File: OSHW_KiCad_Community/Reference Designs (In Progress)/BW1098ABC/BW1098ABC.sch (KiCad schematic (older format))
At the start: 10 parts

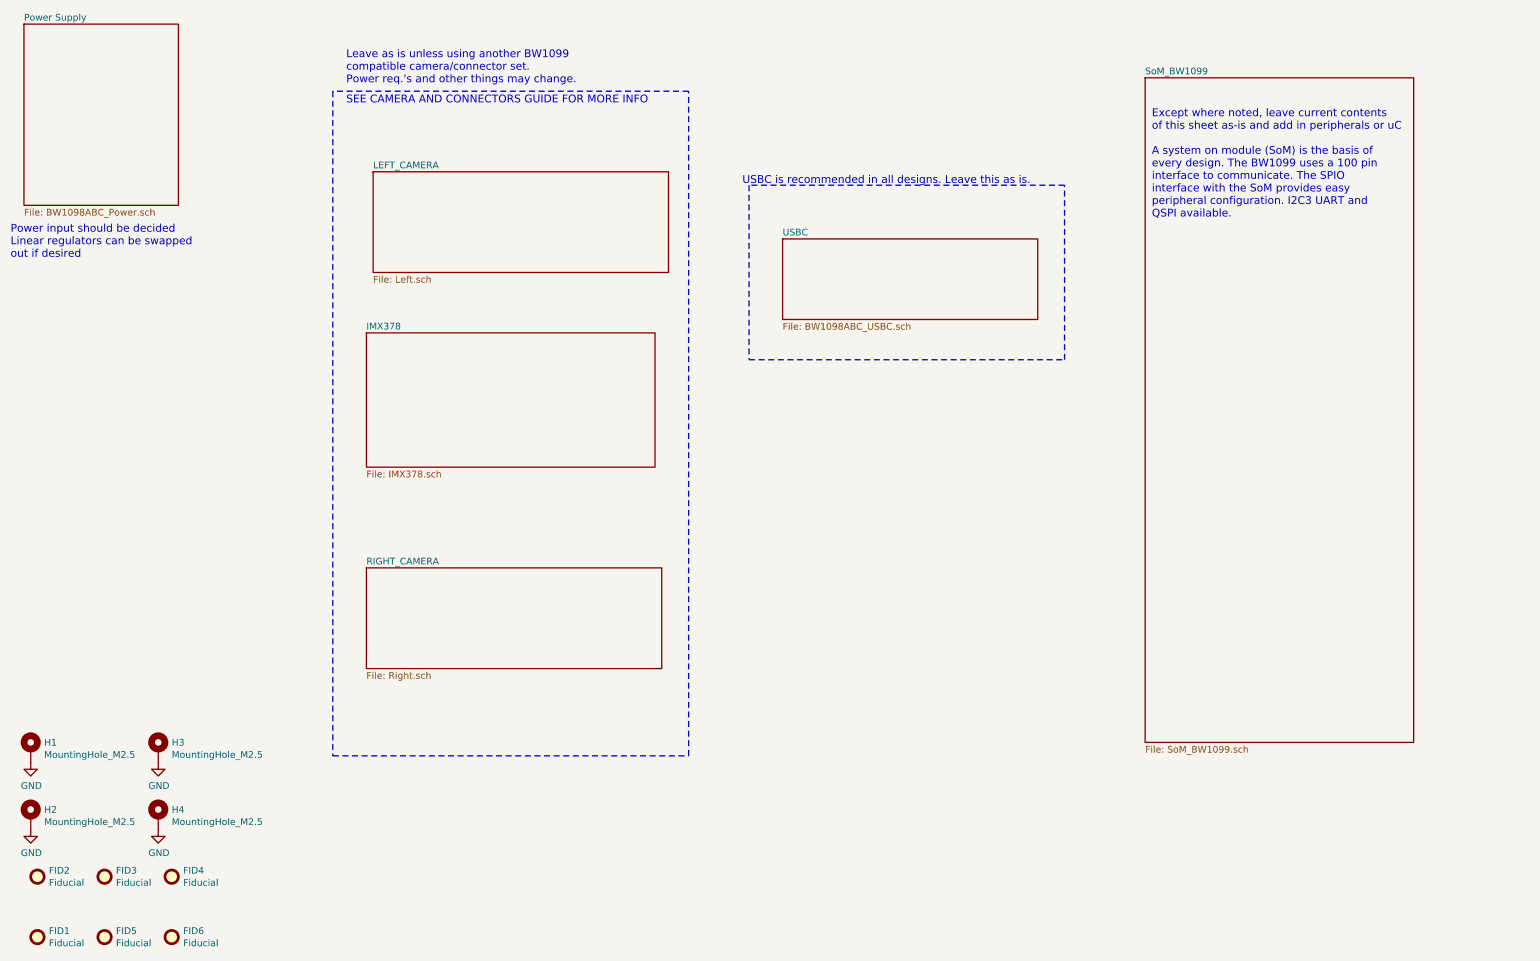
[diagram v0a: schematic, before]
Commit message: switched to ffc design on ABC, dual pop done
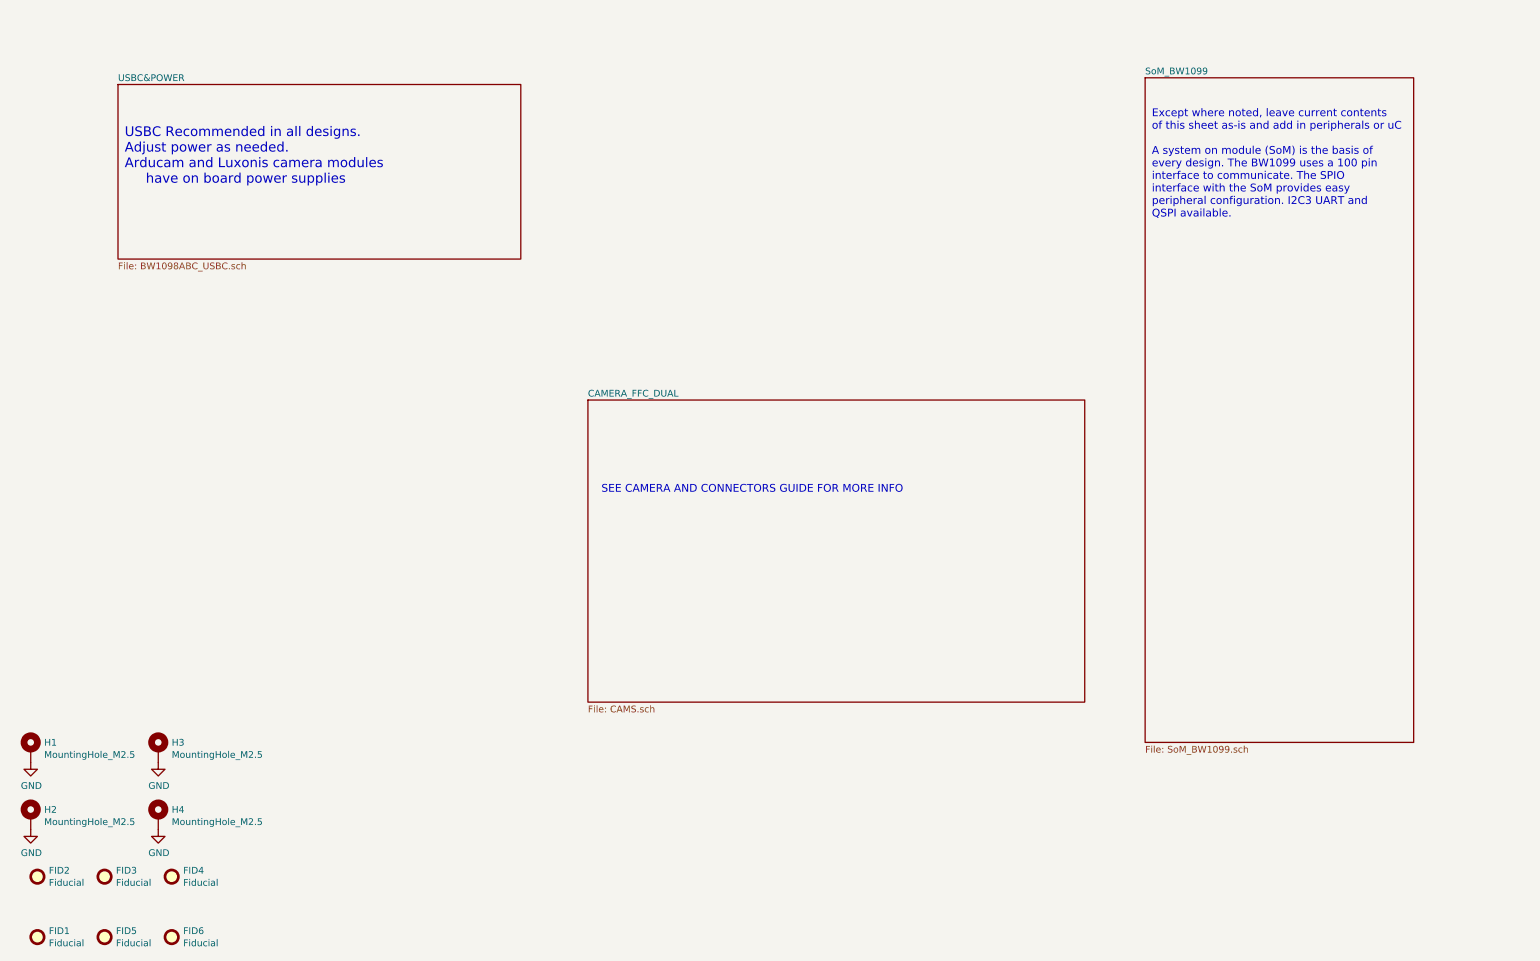
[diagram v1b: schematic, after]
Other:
- note added: "USBC Recommended in all designs. \nAdjust power as needed. \nArducam and Luxonis camera modules \n have on board power supplies"
- note removed: "Leave as is unless using another BW1099 \ncompatible camera/connector set.\nPower req.'s and other things may change."
- note removed: "Power input should be decided\nLinear regulators can be swapped\nout if desired"
- note removed: "USBC is recommended in all designs. Leave this as is.\n"
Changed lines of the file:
@@
 $Descr A4 11693 8268
 encoding utf-8
-Sheet 1 7
+Sheet 1 4
 Title ""
 Date ""
@@
 F0 "SoM_BW1099" 50
 F1 "SoM_BW1099.sch" 50
-$EndSheet
-$Sheet
-S 3150 4650 2200 750
-U 5FF8D40A
-F0 "RIGHT_CAMERA" 50
-F1 "Right.sch" 50
 $EndSheet
 $Comp
@@
 $EndComp
 $Sheet
-S 600  600  1150 1350
-U 604AEAFA
-F0 "Power Supply" 50
-F1 "BW1098ABC_Power.sch" 50
-$EndSheet
-$Sheet
-S 3150 2900 2150 1000
-U 5FF8D4A5
-F0 "IMX378" 50
-F1 "IMX378.sch" 50
-$EndSheet
-$Sheet
-S 3200 1700 2200 750
+S 4800 3400 3700 2250
 U 5FF8D2B3
-F0 "LEFT_CAMERA" 50
-F1 "Left.sch" 50
+F0 "CAMERA_FFC_DUAL" 50
+F1 "CAMS.sch" 50
 $EndSheet
 $Comp
@@
 $EndComp
 $Sheet
-S 6250 2200 1900 600
+S 1300 1050 3000 1300
 U 60483E6B
-F0 "USBC" 50
+F0 "USBC&POWER" 50
 F1 "BW1098ABC_USBC.sch" 50
 $EndSheet
-Wire Notes Line
-	5550 1100 2900 1100
-Wire Notes Line
-	2900 1100 2900 6050
-Wire Notes Line
-	2900 6050 5550 6050
-Wire Notes Line
-	5550 6050 5550 1100
-Text Notes 3000 1200 0    58   ~ 0
+Text Notes 4900 4100 0    58   ~ 0
 SEE CAMERA AND CONNECTORS GUIDE FOR MORE INFO\n
-Wire Notes Line
-	8350 1800 6000 1800
-Wire Notes Line
-	6000 1800 6000 3100
-Wire Notes Line
-	6000 3100 8350 3100
-Wire Notes Line
-	8350 3100 8350 1800
-Text Notes 5950 1800 0    58   ~ 0
-USBC is recommended in all designs. Leave this as is.\n
 Text Notes 9000 2050 0    58   ~ 0
 Except where noted, leave current contents\nof this sheet as-is and add in peripherals or uC\n\nA system on module (SoM) is the basis of \nevery design. The BW1099 uses a 100 pin\ninterface to communicate. The SPIO \ninterface with the SoM provides easy \nperipheral configuration. I2C3 UART and \nQSPI available.
-Text Notes 500  2350 0    58   ~ 0
-Power input should be decided\nLinear regulators can be swapped\nout if desired
-Text Notes 3000 1050 0    58   ~ 0
-Leave as is unless using another BW1099 \ncompatible camera/connector set.\nPower req.'s and other things may change.
+Text Notes 1350 1800 0    72   ~ 0
+USBC Recommended in all designs. \nAdjust power as needed. \nArducam and Luxonis camera modules \n     have on board power supplies
 $EndSCHEMATC

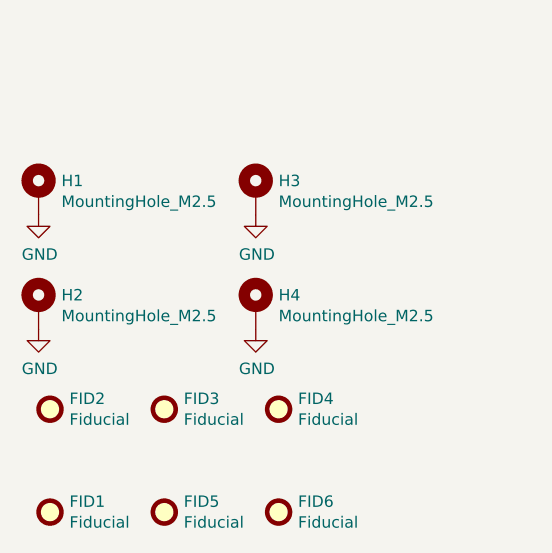
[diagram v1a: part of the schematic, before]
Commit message: added module mounts and started layout for abc
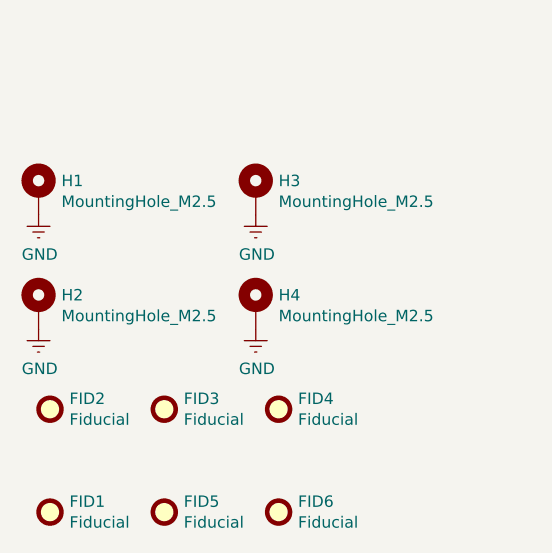
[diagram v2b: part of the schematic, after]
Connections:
- net GND renamed Earth
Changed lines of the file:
@@
 $EndSheet
 $Comp
-L power:GND #PWR0107
+L power:Earth #PWR0107
 U 1 1 6106C817
 P 650 6100
@@
 $EndComp
 $Comp
-L power:GND #PWR0108
+L power:Earth #PWR0108
 U 1 1 6106D903
 P 1600 6100
@@
 $EndComp
 $Comp
-L power:GND #PWR0109
+L power:Earth #PWR0109
 U 1 1 6106E6FC
 P 1600 6600
@@
 $EndComp
 $Comp
-L power:GND #PWR0110
+L power:Earth #PWR0110
 U 1 1 6106EA7D
 P 650 6600

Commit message: layout
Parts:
- added J2: Conn_01x02_Male, Connector_PinHeader_2.54mm:PinHeader_1x02_P2.54mm_Vertical, symbol Connector:Conn_01x02_Male
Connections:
- net Earth: now also J2.1 (Pin_1)
- new net +5V: J2.2 (Pin_2)
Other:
- note added: "FAN CONTROLLER"
- moved on the sheet: FID1, FID2, FID3, FID4, FID5, FID6, H1, H2, H3, H4
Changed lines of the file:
@@
 $EndDescr
 $Sheet
-S 8950 1000 2000 4950
+S 9100 950  2000 4950
 U 5FF8D9B2
 F0 "SoM_BW1099" 50
@@
 L Mechanical:Fiducial FID1
 U 1 1 6049A903
-P 700 7400
-F 0 "FID1" H 785 7446 50  0000 L CNN
-F 1 "Fiducial" H 785 7355 50  0000 L CNN
-F 2 "Fiducial:Fiducial_1mm_Mask2mm" H 700 7400 50  0001 C CNN
-F 3 "~" H 700 7400 50  0001 C CNN
-	1    700  7400
+P 850 7350
+F 0 "FID1" H 935 7396 50  0000 L CNN
+F 1 "Fiducial" H 935 7305 50  0000 L CNN
+F 2 "Fiducial:Fiducial_1mm_Mask2mm" H 850 7350 50  0001 C CNN
+F 3 "~" H 850 7350 50  0001 C CNN
+	1    850  7350
 	1    0    0    -1
 $EndComp
@@
 L Mechanical:Fiducial FID2
 U 1 1 5FF51DEB
-P 700 6950
-F 0 "FID2" H 785 6996 50  0000 L CNN
-F 1 "Fiducial" H 785 6905 50  0000 L CNN
-F 2 "Fiducial:Fiducial_1mm_Mask2mm" H 700 6950 50  0001 C CNN
-F 3 "~" H 700 6950 50  0001 C CNN
-	1    700  6950
+P 850 6900
+F 0 "FID2" H 935 6946 50  0000 L CNN
+F 1 "Fiducial" H 935 6855 50  0000 L CNN
+F 2 "Fiducial:Fiducial_1mm_Mask2mm" H 850 6900 50  0001 C CNN
+F 3 "~" H 850 6900 50  0001 C CNN
+	1    850  6900
 	1    0    0    -1
 $EndComp
@@
 L Mechanical:Fiducial FID3
 U 1 1 6049A905
-P 1200 6950
-F 0 "FID3" H 1285 6996 50  0000 L CNN
-F 1 "Fiducial" H 1285 6905 50  0000 L CNN
-F 2 "Fiducial:Fiducial_1mm_Mask2mm" H 1200 6950 50  0001 C CNN
-F 3 "~" H 1200 6950 50  0001 C CNN
-	1    1200 6950
+P 1350 6900
+F 0 "FID3" H 1435 6946 50  0000 L CNN
+F 1 "Fiducial" H 1435 6855 50  0000 L CNN
+F 2 "Fiducial:Fiducial_1mm_Mask2mm" H 1350 6900 50  0001 C CNN
+F 3 "~" H 1350 6900 50  0001 C CNN
+	1    1350 6900
 	1    0    0    -1
 $EndComp
@@
 L Mechanical:Fiducial FID4
 U 1 1 6049A906
-P 1700 6950
-F 0 "FID4" H 1785 6996 50  0000 L CNN
-F 1 "Fiducial" H 1785 6905 50  0000 L CNN
-F 2 "Fiducial:Fiducial_1mm_Mask2mm" H 1700 6950 50  0001 C CNN
-F 3 "~" H 1700 6950 50  0001 C CNN
-	1    1700 6950
+P 1850 6900
+F 0 "FID4" H 1935 6946 50  0000 L CNN
+F 1 "Fiducial" H 1935 6855 50  0000 L CNN
+F 2 "Fiducial:Fiducial_1mm_Mask2mm" H 1850 6900 50  0001 C CNN
+F 3 "~" H 1850 6900 50  0001 C CNN
+	1    1850 6900
 	1    0    0    -1
 $EndComp
@@
 L Mechanical:Fiducial FID5
 U 1 1 6049A907
-P 1200 7400
-F 0 "FID5" H 1285 7446 50  0000 L CNN
-F 1 "Fiducial" H 1285 7355 50  0000 L CNN
-F 2 "Fiducial:Fiducial_1mm_Mask2mm" H 1200 7400 50  0001 C CNN
-F 3 "~" H 1200 7400 50  0001 C CNN
-	1    1200 7400
+P 1350 7350
+F 0 "FID5" H 1435 7396 50  0000 L CNN
+F 1 "Fiducial" H 1435 7305 50  0000 L CNN
+F 2 "Fiducial:Fiducial_1mm_Mask2mm" H 1350 7350 50  0001 C CNN
+F 3 "~" H 1350 7350 50  0001 C CNN
+	1    1350 7350
 	1    0    0    -1
 $EndComp
@@
 L Mechanical:Fiducial FID6
 U 1 1 600C0C22
-P 1700 7400
-F 0 "FID6" H 1785 7446 50  0000 L CNN
-F 1 "Fiducial" H 1785 7355 50  0000 L CNN
-F 2 "Fiducial:Fiducial_1mm_Mask2mm" H 1700 7400 50  0001 C CNN
-F 3 "~" H 1700 7400 50  0001 C CNN
-	1    1700 7400
+P 1850 7350
+F 0 "FID6" H 1935 7396 50  0000 L CNN
+F 1 "Fiducial" H 1935 7305 50  0000 L CNN
+F 2 "Fiducial:Fiducial_1mm_Mask2mm" H 1850 7350 50  0001 C CNN
+F 3 "~" H 1850 7350 50  0001 C CNN
+	1    1850 7350
 	1    0    0    -1
 $EndComp
@@
 L BW1098ABC-rescue:Mechanical_MountingHole_Pad-depthAI_sch H1
 U 1 1 600C0C23
-P 650 6000
-F 0 "H1" H 750 6049 50  0000 L CNN
-F 1 "MountingHole_M2.5" H 750 5958 50  0000 L CNN
-F 2 "Mounting_Wuerth:Mounting_Wuerth_WA-SMSI-M2_H3mm_9774030243" H 650 6000 50  0001 C CNN
-F 3 "" H 650 6000 50  0001 C CNN
-	1    650  6000
+P 800 5950
+F 0 "H1" H 900 5999 50  0000 L CNN
+F 1 "MountingHole_M2.5" H 900 5908 50  0000 L CNN
+F 2 "Mounting_Wuerth:Mounting_Wuerth_WA-SMSI-M2_H3mm_9774030243" H 800 5950 50  0001 C CNN
+F 3 "" H 800 5950 50  0001 C CNN
+	1    800  5950
 	1    0    0    -1
 $EndComp
@@
 L BW1098ABC-rescue:Mechanical_MountingHole_Pad-depthAI_sch H2
 U 1 1 600C0C24
-P 650 6500
-F 0 "H2" H 750 6549 50  0000 L CNN
-F 1 "MountingHole_M2.5" H 750 6458 50  0000 L CNN
-F 2 "Mounting_Wuerth:Mounting_Wuerth_WA-SMSI-M2_H3mm_9774030243" H 650 6500 50  0001 C CNN
-F 3 "" H 650 6500 50  0001 C CNN
-	1    650  6500
+P 800 6450
+F 0 "H2" H 900 6499 50  0000 L CNN
+F 1 "MountingHole_M2.5" H 900 6408 50  0000 L CNN
+F 2 "Mounting_Wuerth:Mounting_Wuerth_WA-SMSI-M2_H3mm_9774030243" H 800 6450 50  0001 C CNN
+F 3 "" H 800 6450 50  0001 C CNN
+	1    800  6450
 	1    0    0    -1
 $EndComp
@@
 L BW1098ABC-rescue:Mechanical_MountingHole_Pad-depthAI_sch H4
 U 1 1 600C0C25
-P 1600 6500
-F 0 "H4" H 1700 6549 50  0000 L CNN
-F 1 "MountingHole_M2.5" H 1700 6458 50  0000 L CNN
-F 2 "Mounting_Wuerth:Mounting_Wuerth_WA-SMSI-M2_H3mm_9774030243" H 1600 6500 50  0001 C CNN
-F 3 "" H 1600 6500 50  0001 C CNN
-	1    1600 6500
+P 1750 6450
+F 0 "H4" H 1850 6499 50  0000 L CNN
+F 1 "MountingHole_M2.5" H 1850 6408 50  0000 L CNN
+F 2 "Mounting_Wuerth:Mounting_Wuerth_WA-SMSI-M2_H3mm_9774030243" H 1750 6450 50  0001 C CNN
+F 3 "" H 1750 6450 50  0001 C CNN
+	1    1750 6450
 	1    0    0    -1
 $EndComp
@@
 L BW1098ABC-rescue:Mechanical_MountingHole_Pad-depthAI_sch H3
 U 1 1 600C0C26
-P 1600 6000
-F 0 "H3" H 1700 6049 50  0000 L CNN
-F 1 "MountingHole_M2.5" H 1700 5958 50  0000 L CNN
-F 2 "Mounting_Wuerth:Mounting_Wuerth_WA-SMSI-M2_H3mm_9774030243" H 1600 6000 50  0001 C CNN
-F 3 "" H 1600 6000 50  0001 C CNN
-	1    1600 6000
+P 1750 5950
+F 0 "H3" H 1850 5999 50  0000 L CNN
+F 1 "MountingHole_M2.5" H 1850 5908 50  0000 L CNN
+F 2 "Mounting_Wuerth:Mounting_Wuerth_WA-SMSI-M2_H3mm_9774030243" H 1750 5950 50  0001 C CNN
+F 3 "" H 1750 5950 50  0001 C CNN
+	1    1750 5950
 	1    0    0    -1
 $EndComp
 $Sheet
-S 4800 3400 3700 2250
+S 4950 3350 3700 2250
 U 5FF8D2B3
 F0 "CAMERA_FFC_DUAL" 50
@@
 L power:Earth #PWR0107
 U 1 1 6106C817
-P 650 6100
-F 0 "#PWR0107" H 650 5850 50  0001 C CNN
-F 1 "GND" H 655 5927 50  0000 C CNN
-F 2 "" H 650 6100 50  0001 C CNN
-F 3 "" H 650 6100 50  0001 C CNN
-	1    650  6100
+P 800 6050
+F 0 "#PWR0107" H 800 5800 50  0001 C CNN
+F 1 "GND" H 805 5877 50  0000 C CNN
+F 2 "" H 800 6050 50  0001 C CNN
+F 3 "" H 800 6050 50  0001 C CNN
+	1    800  6050
 	1    0    0    -1
 $EndComp
@@
 L power:Earth #PWR0108
 U 1 1 6106D903
-P 1600 6100
-F 0 "#PWR0108" H 1600 5850 50  0001 C CNN
-F 1 "GND" H 1605 5927 50  0000 C CNN
-F 2 "" H 1600 6100 50  0001 C CNN
-F 3 "" H 1600 6100 50  0001 C CNN
-	1    1600 6100
+P 1750 6050
+F 0 "#PWR0108" H 1750 5800 50  0001 C CNN
+F 1 "GND" H 1755 5877 50  0000 C CNN
+F 2 "" H 1750 6050 50  0001 C CNN
+F 3 "" H 1750 6050 50  0001 C CNN
+	1    1750 6050
 	1    0    0    -1
 $EndComp
@@
 L power:Earth #PWR0109
 U 1 1 6106E6FC
-P 1600 6600
-F 0 "#PWR0109" H 1600 6350 50  0001 C CNN
-F 1 "GND" H 1605 6427 50  0000 C CNN
-F 2 "" H 1600 6600 50  0001 C CNN
-F 3 "" H 1600 6600 50  0001 C CNN
-	1    1600 6600
+P 1750 6550
+F 0 "#PWR0109" H 1750 6300 50  0001 C CNN
+F 1 "GND" H 1755 6377 50  0000 C CNN
+F 2 "" H 1750 6550 50  0001 C CNN
+F 3 "" H 1750 6550 50  0001 C CNN
+	1    1750 6550
 	1    0    0    -1
 $EndComp
@@
 L power:Earth #PWR0110
 U 1 1 6106EA7D
-P 650 6600
-F 0 "#PWR0110" H 650 6350 50  0001 C CNN
-F 1 "GND" H 655 6427 50  0000 C CNN
-F 2 "" H 650 6600 50  0001 C CNN
-F 3 "" H 650 6600 50  0001 C CNN
-	1    650  6600
+P 800 6550
+F 0 "#PWR0110" H 800 6300 50  0001 C CNN
+F 1 "GND" H 805 6377 50  0000 C CNN
+F 2 "" H 800 6550 50  0001 C CNN
+F 3 "" H 800 6550 50  0001 C CNN
+	1    800  6550
 	1    0    0    -1
 $EndComp
 $Sheet
-S 1300 1050 3000 1300
+S 1450 1000 3000 1300
 U 60483E6B
 F0 "USBC&POWER" 50
 F1 "BW1098ABC_USBC.sch" 50
 $EndSheet
-Text Notes 4900 4100 0    58   ~ 0
+Text Notes 5050 4050 0    58   ~ 0
 SEE CAMERA AND CONNECTORS GUIDE FOR MORE INFO\n
-Text Notes 9000 2050 0    58   ~ 0
+Text Notes 9150 2000 0    58   ~ 0
 Except where noted, leave current contents\nof this sheet as-is and add in peripherals or uC\n\nA system on module (SoM) is the basis of \nevery design. The BW1099 uses a 100 pin\ninterface to communicate. The SPIO \ninterface with the SoM provides easy \nperipheral configuration. I2C3 UART and \nQSPI available.
-Text Notes 1350 1800 0    72   ~ 0
+Text Notes 1500 1750 0    72   ~ 0
 USBC Recommended in all designs. \nAdjust power as needed. \nArducam and Luxonis camera modules \n     have on board power supplies
+$Comp
+L power:Earth #GND_?
+U 1 1 60A13627
+P 2150 4050
+AR Path="/5FD7EFCB/60A13627" Ref="#GND_?"  Part="1"
+AR Path="/604AEAFA/60A13627" Ref="#GND_?"  Part="1"
+AR Path="/60483E6B/60A13627" Ref="#GND_?"  Part="1"
+AR Path="/60A13627" Ref="#GND_0101"  Part="1"
+F 0 "#GND_0101" H 2150 4050 20  0000 C CNN
+F 1 "GND" H 2150 3980 30  0000 C CNN
+F 2 "" H 2150 4050 70  0000 C CNN
+F 3 "" H 2150 4050 70  0000 C CNN
+	1    2150 4050
+	1    0    0    -1
+$EndComp
+Text Notes 1800 4550 0    120  ~ 24
+FAN CONTROLLER
+Wire Wire Line
+	2300 4050 2150 4050
+$Comp
+L power:+5V #PWR?
+U 1 1 60A1362F
+P 1550 3900
+AR Path="/60483E6B/60A1362F" Ref="#PWR?"  Part="1"
+AR Path="/60A1362F" Ref="#PWR0111"  Part="1"
+F 0 "#PWR0111" H 1550 3750 50  0001 C CNN
+F 1 "+5V" H 1565 4073 50  0000 C CNN
+F 2 "" H 1550 3900 50  0001 C CNN
+F 3 "" H 1550 3900 50  0001 C CNN
+	1    1550 3900
+	1    0    0    -1
+$EndComp
+Wire Wire Line
+	1550 3950 1550 3900
+Wire Wire Line
+	1550 3950 2300 3950
+Wire Notes Line
+	3600 3550 1300 3550
+Wire Notes Line
+	1300 3550 1300 4600
+Wire Notes Line
+	1300 4600 3600 4600
+Wire Notes Line
+	3600 4600 3600 3550
+$Comp
+L Connector:Conn_01x02_Male J?
+U 1 1 60A1363B
+P 2500 4050
+AR Path="/60483E6B/60A1363B" Ref="J?"  Part="1"
+AR Path="/60A1363B" Ref="J2"  Part="1"
+F 0 "J2" H 2472 3932 50  0000 R CNN
+F 1 "Conn_01x02_Male" H 2472 4023 50  0000 R CNN
+F 2 "Connector_PinHeader_2.54mm:PinHeader_1x02_P2.54mm_Vertical" H 2500 4050 50  0001 C CNN
+F 3 "~" H 2500 4050 50  0001 C CNN
+	1    2500 4050
+	-1   0    0    1
+$EndComp
 $EndSCHEMATC

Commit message: ABC Updates
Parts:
- J2: footprint Connector_PinHeader_2.54mm:PinHeader_1x02_P2.54mm_Vertical -> Connector_JST:JST_GH_BM02B-GHS-TBT_1x02-1MP_P1.25mm_Vertical
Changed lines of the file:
@@
 $EndComp
 $Sheet
-S 4950 3350 3700 2250
+S 4500 3050 3700 2250
 U 5FF8D2B3
 F0 "CAMERA_FFC_DUAL" 50
@@
 F1 "BW1098ABC_USBC.sch" 50
 $EndSheet
-Text Notes 5050 4050 0    58   ~ 0
+Text Notes 4600 3750 0    58   ~ 0
 SEE CAMERA AND CONNECTORS GUIDE FOR MORE INFO\n
 Text Notes 9150 2000 0    58   ~ 0
@@
 F 0 "J2" H 2472 3932 50  0000 R CNN
 F 1 "Conn_01x02_Male" H 2472 4023 50  0000 R CNN
-F 2 "Connector_PinHeader_2.54mm:PinHeader_1x02_P2.54mm_Vertical" H 2500 4050 50  0001 C CNN
+F 2 "Connector_JST:JST_GH_BM02B-GHS-TBT_1x02-1MP_P1.25mm_Vertical" H 2500 4050 50  0001 C CNN
 F 3 "~" H 2500 4050 50  0001 C CNN
 	1    2500 4050
